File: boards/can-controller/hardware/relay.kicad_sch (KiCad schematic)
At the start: 28 parts, among them J30 RELAY, U30 ISO6740, U31 ISO6740, U32 ULN2803A, U33 MCP23008-E/SO

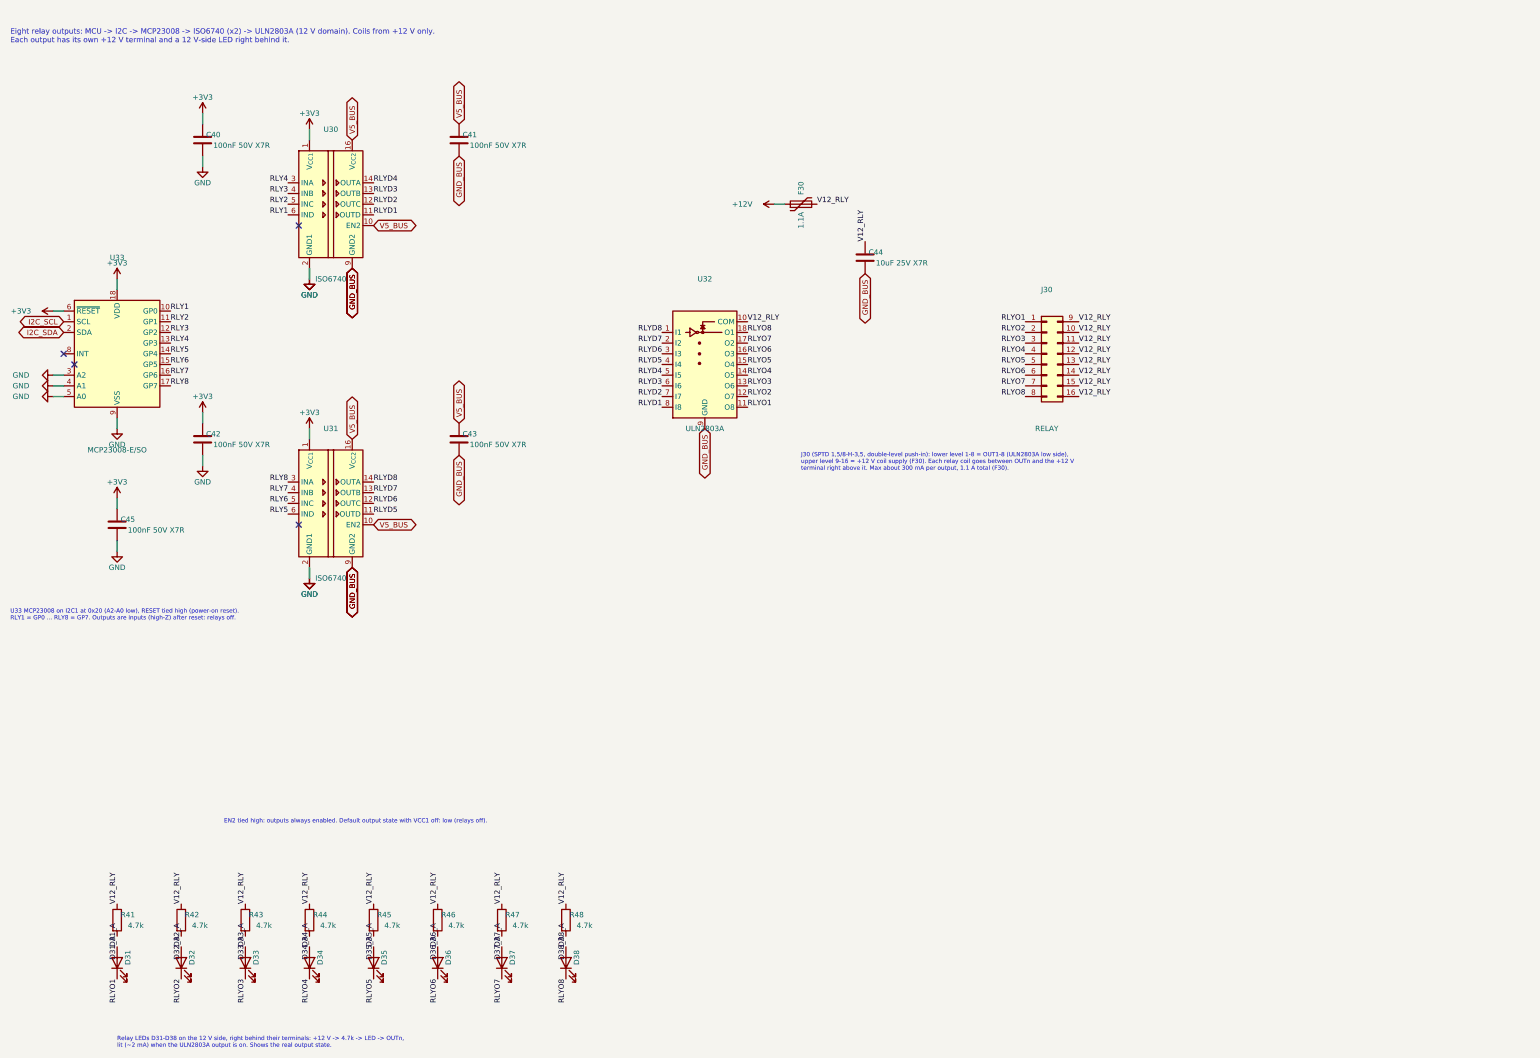
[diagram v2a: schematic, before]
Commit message: can-controller: schematic for the new scope (Ethernet W6100, 4 x ISOW1044, AQW212 relays, diff AI)
Six sheets generated by gen_schematic.py: MCU and logic power, Ethernet,
CAN x4, 12 V input and isolated logic supply (TDN 5-2411WI), relay drive,
GPIO and analog in. ERC 0; netlist check: no net crosses a domain except
at the designed crossings. New lib parts: Thl_Interface:W6100-L (flat),
Thl_Isolator:AQW212, stock ISOW1044 / TDN 5WI / LQFP-48 / bead footprints.
PCB still holds the old layout (next: update from schematic, placement).

Co-Authored-By: Claude Opus 5.5 <noreply@anthropic.com>
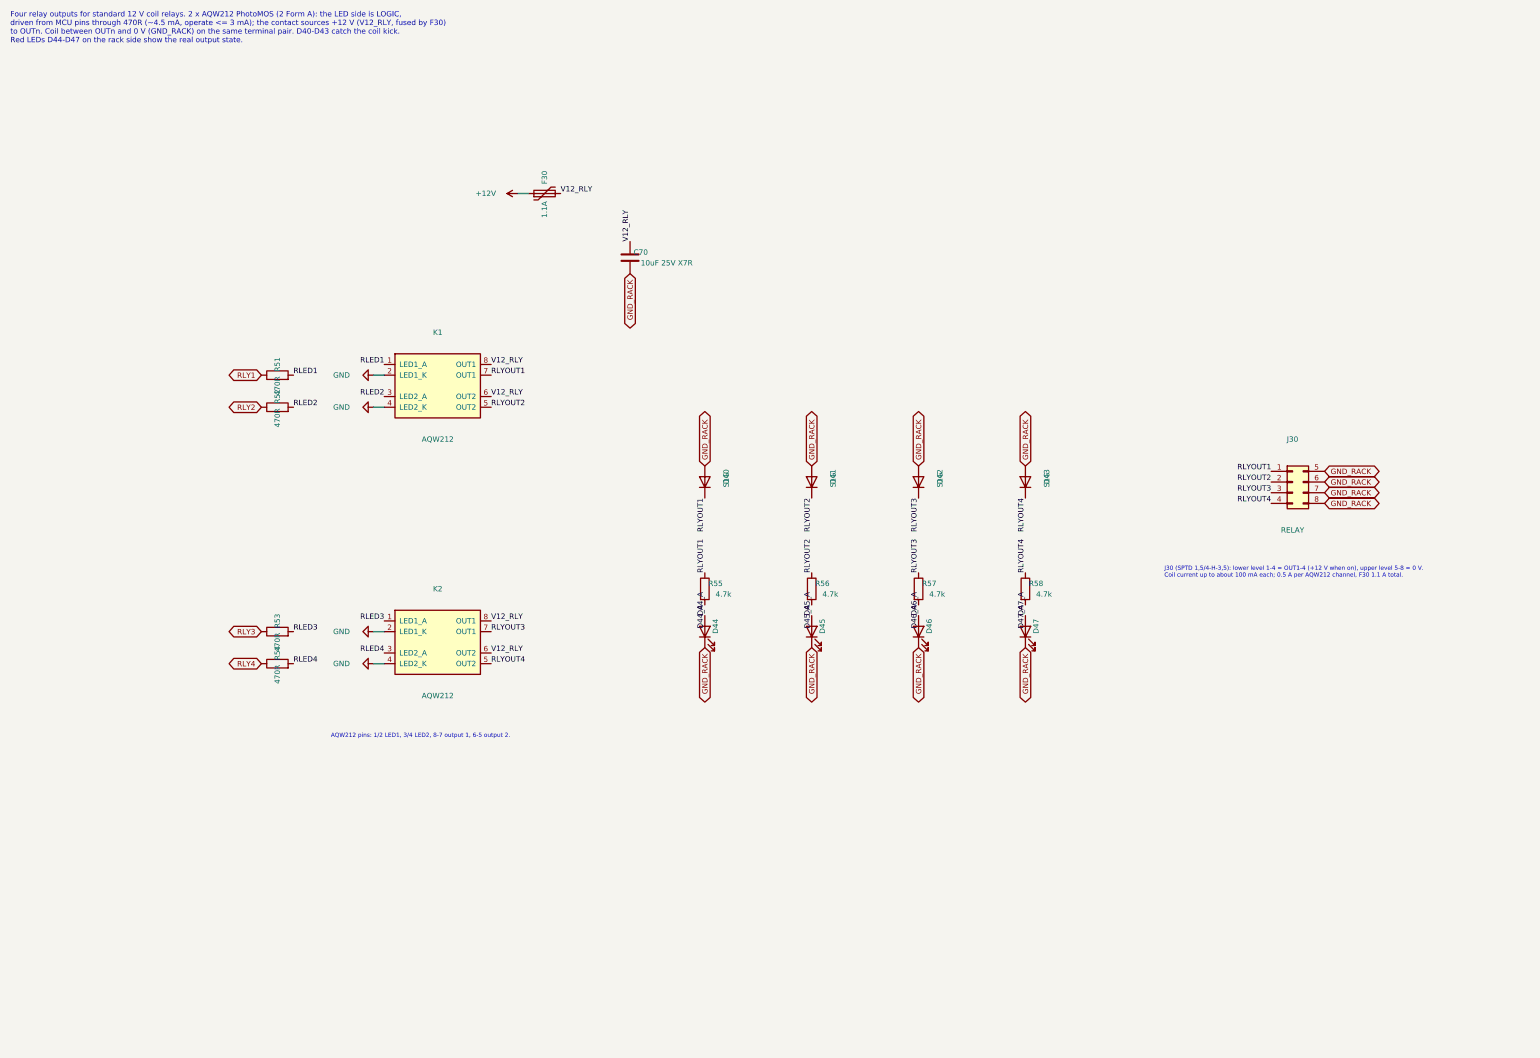
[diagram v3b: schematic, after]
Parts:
- removed C40, C41, C42, C43, C45: 100nF 50V X7R, Capacitor_SMD:C_0805_2012Metric_Pad1.18x1.45mm_HandSolder, symbol Device:C
- removed C44: 10uF 25V X7R, Capacitor_SMD:C_1206_3216Metric_Pad1.33x1.80mm_HandSolder, symbol Device:C
- removed D31, D32, D33, D34, D35, D36, D37, D38: LED red, LED_SMD:LED_1206_3216Metric_Pad1.42x1.75mm_HandSolder, symbol Device:LED
- removed J30: RELAY, Thl_Connector:PhoenixContact_SPTD_1,5_8-H-3,5_2x08_P3.5mm_Horizontal, symbol Connector_Generic:Conn_02x08_Top_Bottom
- removed R41, R42, R43, R44, R45, R46, R47, R48: 4.7k, Resistor_SMD:R_1206_3216Metric_Pad1.30x1.75mm_HandSolder, symbol Device:R
- removed U30, U31: ISO6740, Package_SO:SOIC-16W_7.5x10.3mm_P1.27mm, symbol Isolator:ISO6740
- removed U32: ULN2803A, Package_SO:SOIC-18W_7.5x11.6mm_P1.27mm, symbol Transistor_Array:ULN2803A
- removed U33: MCP23008-E/SO, Package_SO:SOIC-18W_7.5x11.6mm_P1.27mm, symbol Interface_Expansion:MCP23008-xSO
- added C70: 10uF 25V X7R, Capacitor_SMD:C_1206_3216Metric_Pad1.33x1.80mm_HandSolder, symbol Device:C
- added D40, D41, D42, D43: S1G, Diode_SMD:D_SMA_Handsoldering, symbol Device:D
- added D44, D45, D46, D47: LED red, LED_SMD:LED_1206_3216Metric_Pad1.42x1.75mm_HandSolder, symbol Device:LED
- added J30: RELAY, Thl_Connector:PhoenixContact_SPTD_1,5_4-H-3,5_2x04_P3.5mm_Horizontal, symbol Connector_Generic:Conn_02x04_Top_Bottom
- added K1, K2: AQW212, Package_DIP:DIP-8_W7.62mm, symbol Thl_Isolator:AQW212
- added R51, R52, R53, R54: 470R, Resistor_SMD:R_1206_3216Metric_Pad1.30x1.75mm_HandSolder, symbol Device:R
- added R55, R56, R57, R58: 4.7k, Resistor_SMD:R_1206_3216Metric_Pad1.30x1.75mm_HandSolder, symbol Device:R
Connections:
- net GND: now also K1.2 (LED1_K), K1.4 (LED2_K), K2.2 (LED1_K), K2.4 (LED2_K)
- net RLY1: now also R51.1
- net RLY2: now also R52.1
- net RLY3: now also R53.1
- net RLY4: now also R54.1
- net V12_RLY: now also C70.1, K1.6 (OUT2), K1.8 (OUT1), K2.6 (OUT2), K2.8 (OUT1)
- new net D44_A: D44.2 (A), R55.2
- new net D45_A: D45.2 (A), R56.2
- new net D46_A: D46.2 (A), R57.2
- new net D47_A: D47.2 (A), R58.2
- new net GND_RACK: C70.2, D40.2 (A), D41.2 (A), D42.2 (A), D43.2 (A), D44.1 (K), D45.1 (K), D46.1 (K), D47.1 (K), J30.5 (Pin_5), J30.6 (Pin_6), J30.7 (Pin_7), J30.8 (Pin_8)
- new net RLED1: K1.1 (LED1_A), R51.2
- new net RLED2: K1.3 (LED2_A), R52.2
- new net RLED3: K2.1 (LED1_A), R53.2
- new net RLED4: K2.3 (LED2_A), R54.2
- new net RLYOUT1: D40.1 (K), J30.1 (Pin_1), K1.7 (OUT1), R55.1
- new net RLYOUT2: D41.1 (K), J30.2 (Pin_2), K1.5 (OUT2), R56.1
- new net RLYOUT3: D42.1 (K), J30.3 (Pin_3), K2.7 (OUT1), R57.1
- new net RLYOUT4: D43.1 (K), J30.4 (Pin_4), K2.5 (OUT2), R58.1
- no-connect marks 4 -> 0
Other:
- note added: "AQW212 pins: 1/2 LED1, 3/4 LED2, 8-7 output 1, 6-5 output 2."
- note added: "Four relay outputs for standard 12 V coil relays. 2 x AQW212 PhotoMOS (2 Form A): the LED side is LOGIC, driven from MCU pins through 470R (~4.5 mA, operate <= 3 mA); the contact sources +12 V (V12_RLY, fused by F30) to OUTn. Coil between OUTn and 0 V (GND_RACK) on the same terminal pair. D40-D43 catch the coil kick. Red LEDs D44-D47 on the rack side show the real output state."
- note added: "J30 (SPTD 1,5/4-H-3,5): lower level 1-4 = OUT1-4 (+12 V when on), upper level 5-8 = 0 V. Coil current up to about 100 mA each; 0.5 A per AQW212 channel, F30 1.1 A total."
- note removed: "EN2 tied high: outputs always enabled. Default output state with VCC1 off: low (relays off)."
- note removed: "Eight relay outputs: MCU -> I2C -> MCP23008 -> ISO6740 (x2) -> ULN2803A (12 V domain). Coils from +12 V only. Each output has its own +12 V terminal and a 12 V-side LED right behind it."
- note removed: "J30 (SPTD 1,5/8-H-3,5, double-level push-in): lower level 1-8 = OUT1-8 (ULN2803A low side), upper level 9-16 = +12 V coil supply (F30). Each relay coil goes between OUTn and the +12 V terminal right above it. Max about 300 mA per output, 1.1 A total (F30)."
- note removed: "Relay LEDs D31-D38 on the 12 V side, right behind their terminals: +12 V -> 4.7k -> LED -> OUTn, lit (~2 mA) when the ULN2803A output is on. Shows the real output state."
- note removed: "U33 MCP23008 on I2C1 at 0x20 (A2-A0 low), RESET tied high (power-on reset). RLY1 = GP0 ... RLY8 = GP7. Outputs are inputs (high-Z) after reset: relays off."
